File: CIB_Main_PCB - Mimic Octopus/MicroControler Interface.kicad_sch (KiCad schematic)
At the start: 3 parts

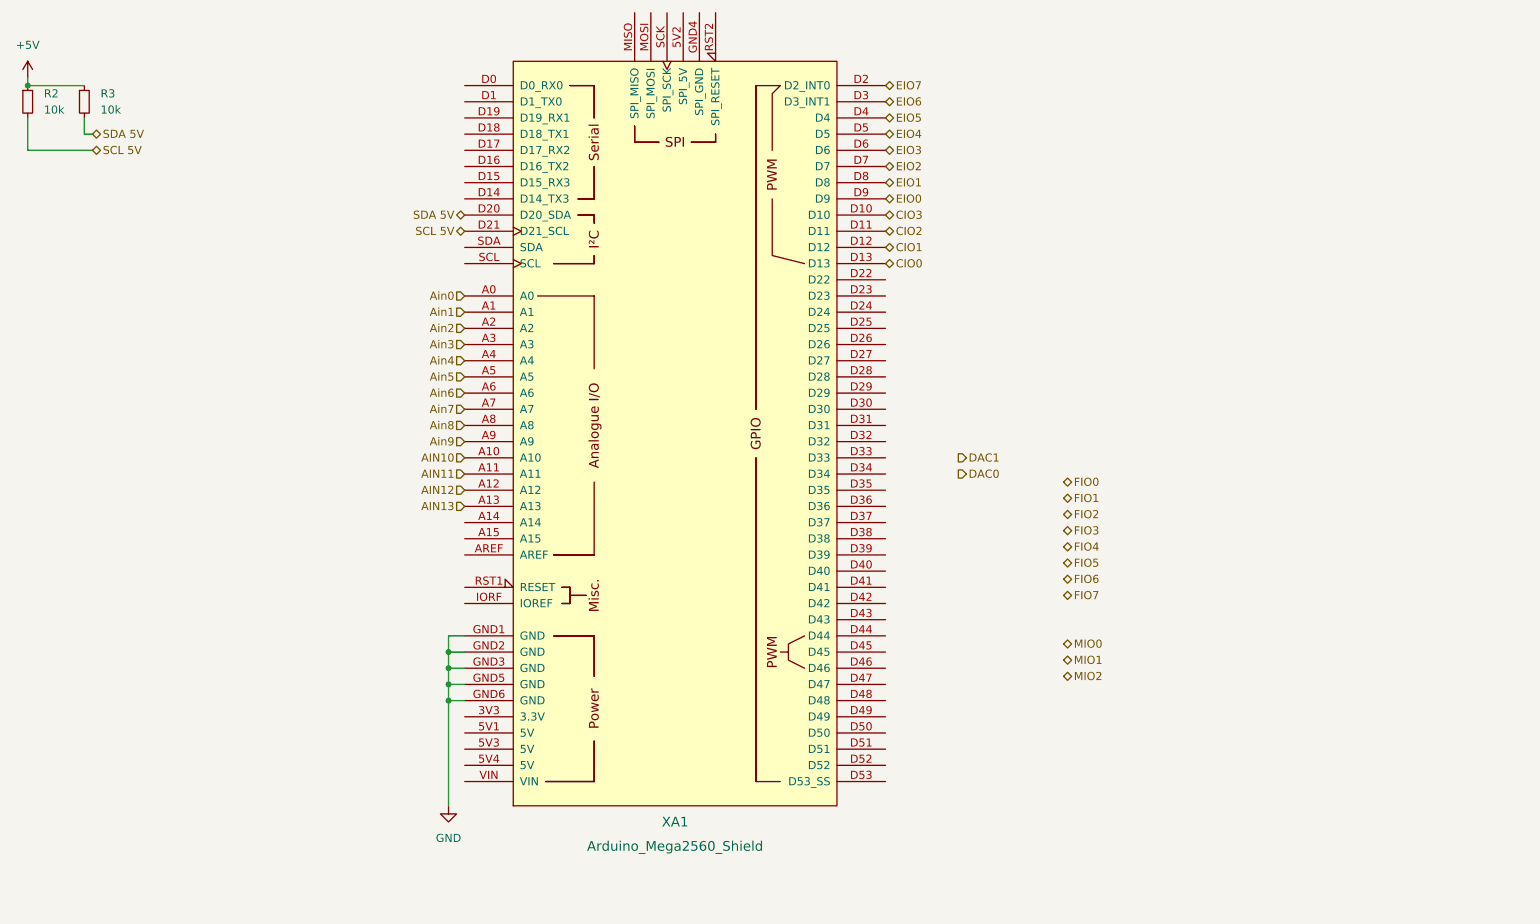
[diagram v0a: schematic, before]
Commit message: Added revision resistors
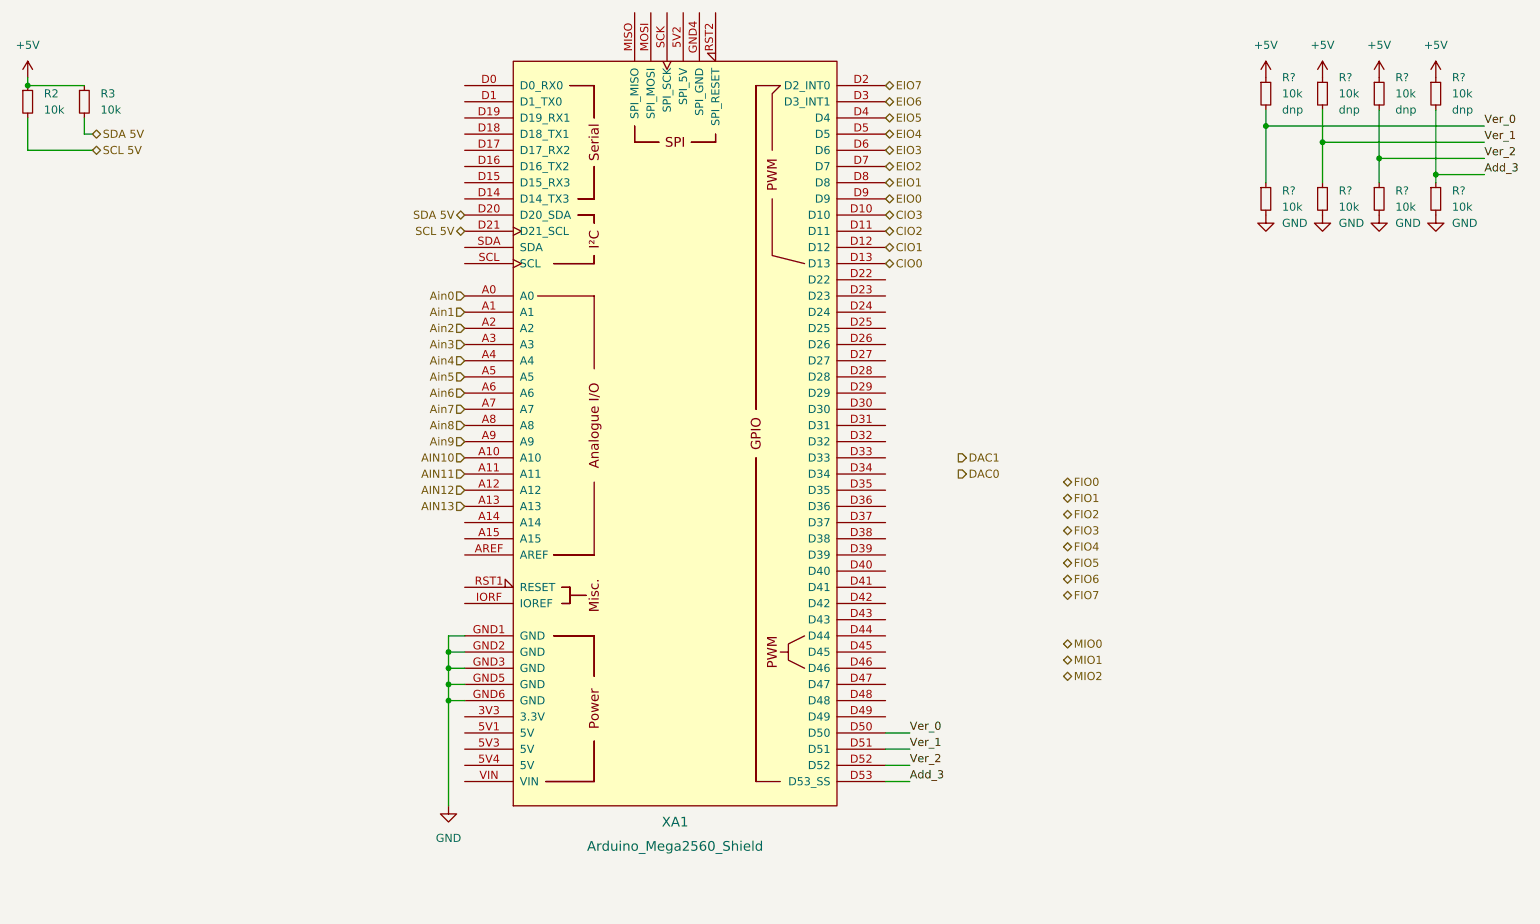
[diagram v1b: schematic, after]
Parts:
- added R? (x8): 10k, Resistor_SMD:R_1206_3216Metric_Pad1.30x1.75mm_HandSolder, symbol Device:R_Small
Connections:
- net +5V: now also R?.1, R?.1, R?.1, R?.1
- net GND: now also R?.2, R?.2, R?.2, R?.2
- net Ver_0: now reaches XA1.D50
- net Ver_0: now also R?.1, R?.2
- net Ver_1: now reaches XA1.D51
- net Ver_1: now also R?.1, R?.2
- net Ver_2: now reaches XA1.D52
- net Ver_2: now also R?.1, R?.2
- net Add_3: now reaches XA1.D53 (D53_SS)
- net Add_3: now also R?.1, R?.2

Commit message: added version resistors
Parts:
- gave numbers to parts that had none: 8
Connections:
- net Ver_0: now also XA1.D46; no longer XA1.D50
- net Ver_1: now also XA1.D48; no longer XA1.D51
- net Ver_2: now also XA1.D50; no longer XA1.D52
- net Add_3 renamed Ver_3
- net Ver_3: now also XA1.D52; no longer XA1.D53 (D53_SS)
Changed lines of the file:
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@@
+    (stroke (width 0) (type default) (color 0 0 0 0))
+  )
+  (wire (pts (xy 152.4 121.92) (xy 156.21 121.92))
     (stroke (width 0) (type default) (color 0 0 0 0))
   )
@@
     (stroke (width 0) (type default) (color 0 0 0 0))
   )
+  (wire (pts (xy 152.4 116.84) (xy 156.21 116.84))
+    (stroke (width 0) (type default) (color 0 0 0 0))
+  )
   (wire (pts (xy 83.82 121.92) (xy 86.36 121.92))
     (stroke (width 0) (type default) (color 0 0 0 0))
   )
-  (wire (pts (xy 152.4 129.54) (xy 156.21 129.54))
-    (stroke (width 0) (type default) (color 0 0 0 0))
-  )
   (wire (pts (xy 229.87 36.83) (xy 229.87 40.64))
     (stroke (width 0) (type default) (color 0 0 0 0))
@@
     (stroke (width 0) (type default) (color 0 0 0 0))
   )
-  (wire (pts (xy 152.4 134.62) (xy 156.21 134.62))
-    (stroke (width 0) (type default) (color 0 0 0 0))
-  )
   (wire (pts (xy 83.82 114.3) (xy 86.36 114.3))
     (stroke (width 0) (type default) (color 0 0 0 0))
@@
     (stroke (width 0) (type default) (color 0 0 0 0))
   )
-  (label "Ver_2" (at 156.21 132.08 0)
+  (label "Ver_2" (at 156.21 127 0)
     (effects (font (size 1.27 1.27)) (justify left bottom))
   )
-  (label "Add_3" (at 246.38 39.37 0)
+  (label "Ver_3" (at 246.38 39.37 0)
     (effects (font (size 1.27 1.27)) (justify left bottom))
   )
-  (label "Ver_0" (at 156.21 127 0)
+  (label "Ver_3" (at 156.21 132.08 0)
     (effects (font (size 1.27 1.27)) (justify left bottom))
   )
-  (label "Add_3" (at 156.21 134.62 0)
+  (label "Ver_0" (at 156.21 116.84 0)
     (effects (font (size 1.27 1.27)) (justify left bottom))
   )
@@
     (effects (font (size 1.27 1.27)) (justify left bottom))
   )
-  (label "Ver_1" (at 156.21 129.54 0)
+  (label "Ver_1" (at 156.21 121.92 0)
     (effects (font (size 1.27 1.27)) (justify left bottom))
   )
@@
   (symbol (lib_id "power:GND") (at 220.98 45.72 0) (unit 1)
     (in_bom yes) (on_board yes) (fields_autoplaced)
-    (property "Reference" "#PWR?" (id 0) (at 220.98 52.07 0)
+    (property "Reference" "#PWR0421" (id 0) (at 220.98 52.07 0)
       (effects (font (size 1.27 1.27)) hide)
     )
@@
   (symbol (lib_id "power:GND") (at 238.76 45.72 0) (unit 1)
     (in_bom yes) (on_board yes) (fields_autoplaced)
-    (property "Reference" "#PWR?" (id 0) (at 238.76 52.07 0)
+    (property "Reference" "#PWR0427" (id 0) (at 238.76 52.07 0)
       (effects (font (size 1.27 1.27)) hide)
     )
@@
   (symbol (lib_id "power:+5V") (at 238.76 24.13 0) (unit 1)
     (in_bom yes) (on_board yes) (fields_autoplaced)
-    (property "Reference" "#PWR?" (id 0) (at 238.76 27.94 0)
+    (property "Reference" "#PWR0422" (id 0) (at 238.76 27.94 0)
       (effects (font (size 1.27 1.27)) hide)
     )
@@
   (symbol (lib_id "Device:R_Small") (at 238.76 26.67 0) (unit 1)
     (in_bom yes) (on_board yes) (fields_autoplaced)
-    (property "Reference" "R?" (id 0) (at 241.3 24.1299 0)
+    (property "Reference" "R55" (id 0) (at 241.3 24.1299 0)
       (effects (font (size 1.27 1.27)) (justify left))
     )
@@
   (symbol (lib_id "Device:R_Small") (at 229.87 43.18 0) (unit 1)
     (in_bom yes) (on_board yes) (fields_autoplaced)
-    (property "Reference" "R?" (id 0) (at 232.41 41.9099 0)
+    (property "Reference" "R58" (id 0) (at 232.41 41.9099 0)
       (effects (font (size 1.27 1.27)) (justify left))
     )
@@
   (symbol (lib_id "power:+5V") (at 212.09 24.13 0) (unit 1)
     (in_bom yes) (on_board yes) (fields_autoplaced)
-    (property "Reference" "#PWR?" (id 0) (at 212.09 27.94 0)
+    (property "Reference" "#PWR0424" (id 0) (at 212.09 27.94 0)
       (effects (font (size 1.27 1.27)) hide)
     )
@@
   (symbol (lib_id "power:+5V") (at 220.98 24.13 0) (unit 1)
     (in_bom yes) (on_board yes) (fields_autoplaced)
-    (property "Reference" "#PWR?" (id 0) (at 220.98 27.94 0)
+    (property "Reference" "#PWR0423" (id 0) (at 220.98 27.94 0)
       (effects (font (size 1.27 1.27)) hide)
     )
@@
   (symbol (lib_id "power:GND") (at 229.87 45.72 0) (unit 1)
     (in_bom yes) (on_board yes) (fields_autoplaced)
-    (property "Reference" "#PWR?" (id 0) (at 229.87 52.07 0)
+    (property "Reference" "#PWR0426" (id 0) (at 229.87 52.07 0)
       (effects (font (size 1.27 1.27)) hide)
     )
@@
   (symbol (lib_id "power:GND") (at 212.09 45.72 0) (unit 1)
     (in_bom yes) (on_board yes) (fields_autoplaced)
-    (property "Reference" "#PWR?" (id 0) (at 212.09 52.07 0)
+    (property "Reference" "#PWR0420" (id 0) (at 212.09 52.07 0)
       (effects (font (size 1.27 1.27)) hide)
     )
@@
   (symbol (lib_id "Device:R_Small") (at 238.76 43.18 0) (unit 1)
     (in_bom yes) (on_board yes) (fields_autoplaced)
-    (property "Reference" "R?" (id 0) (at 241.3 41.9099 0)
+    (property "Reference" "R59" (id 0) (at 241.3 41.9099 0)
       (effects (font (size 1.27 1.27)) (justify left))
     )
@@
   (symbol (lib_id "Device:R_Small") (at 220.98 43.18 0) (unit 1)
     (in_bom yes) (on_board yes) (fields_autoplaced)
-    (property "Reference" "R?" (id 0) (at 223.52 41.9099 0)
+    (property "Reference" "R57" (id 0) (at 223.52 41.9099 0)
       (effects (font (size 1.27 1.27)) (justify left))
     )
@@
   (symbol (lib_id "Device:R_Small") (at 229.87 26.67 0) (unit 1)
     (in_bom yes) (on_board yes) (fields_autoplaced)
-    (property "Reference" "R?" (id 0) (at 232.41 24.1299 0)
+    (property "Reference" "R54" (id 0) (at 232.41 24.1299 0)
       (effects (font (size 1.27 1.27)) (justify left))
     )
@@
   (symbol (lib_id "Device:R_Small") (at 212.09 26.67 0) (unit 1)
     (in_bom yes) (on_board yes) (fields_autoplaced)
-    (property "Reference" "R?" (id 0) (at 214.63 24.1299 0)
+    (property "Reference" "R40" (id 0) (at 214.63 24.1299 0)
       (effects (font (size 1.27 1.27)) (justify left))
     )
@@
   (symbol (lib_id "Device:R_Small") (at 212.09 43.18 0) (unit 1)
     (in_bom yes) (on_board yes) (fields_autoplaced)
-    (property "Reference" "R?" (id 0) (at 214.63 41.9099 0)
+    (property "Reference" "R56" (id 0) (at 214.63 41.9099 0)
       (effects (font (size 1.27 1.27)) (justify left))
     )
@@
   (symbol (lib_id "Device:R_Small") (at 220.98 26.67 0) (unit 1)
     (in_bom yes) (on_board yes) (fields_autoplaced)
-    (property "Reference" "R?" (id 0) (at 223.52 24.1299 0)
+    (property "Reference" "R52" (id 0) (at 223.52 24.1299 0)
       (effects (font (size 1.27 1.27)) (justify left))
     )
@@
   (symbol (lib_id "power:+5V") (at 229.87 24.13 0) (unit 1)
     (in_bom yes) (on_board yes) (fields_autoplaced)
-    (property "Reference" "#PWR?" (id 0) (at 229.87 27.94 0)
-      (effects (font (size 1.27 1.27)) hide)
-    )
+    (property "Reference" "#PWR0425" (id 0) (at 229.87 27.94 0)
+      (effects (font (size 1.27 1.27)) hide)
+    )

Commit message: added changes
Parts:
- renumbered R40 to R1, R59 to R10, R52 to R2, R54 to R3, R55 to R4, R2 to R5, R3 to R6, R56 to R7, R57 to R8, R58 to R9
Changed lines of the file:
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@@
   (symbol (lib_id "power:GND") (at 220.98 45.72 0) (unit 1)
     (in_bom yes) (on_board yes) (fields_autoplaced)
-    (property "Reference" "#PWR0421" (id 0) (at 220.98 52.07 0)
+    (property "Reference" "#PWR038" (id 0) (at 220.98 52.07 0)
       (effects (font (size 1.27 1.27)) hide)
     )
@@
   (symbol (lib_id "power:GND") (at 238.76 45.72 0) (unit 1)
     (in_bom yes) (on_board yes) (fields_autoplaced)
-    (property "Reference" "#PWR0427" (id 0) (at 238.76 52.07 0)
+    (property "Reference" "#PWR040" (id 0) (at 238.76 52.07 0)
       (effects (font (size 1.27 1.27)) hide)
     )
@@
   (symbol (lib_id "Device:R_Small") (at 26.67 27.94 0) (unit 1)
     (in_bom yes) (on_board yes) (fields_autoplaced)
-    (property "Reference" "R3" (id 0) (at 29.21 26.6699 0)
+    (property "Reference" "R6" (id 0) (at 29.21 26.6699 0)
       (effects (font (size 1.27 1.27)) (justify left))
     )
@@
   (symbol (lib_id "power:+5V") (at 238.76 24.13 0) (unit 1)
     (in_bom yes) (on_board yes) (fields_autoplaced)
-    (property "Reference" "#PWR0422" (id 0) (at 238.76 27.94 0)
+    (property "Reference" "#PWR036" (id 0) (at 238.76 27.94 0)
       (effects (font (size 1.27 1.27)) hide)
     )
@@
   (symbol (lib_id "Device:R_Small") (at 17.78 27.94 0) (unit 1)
     (in_bom yes) (on_board yes) (fields_autoplaced)
-    (property "Reference" "R2" (id 0) (at 20.32 26.6699 0)
+    (property "Reference" "R5" (id 0) (at 20.32 26.6699 0)
       (effects (font (size 1.27 1.27)) (justify left))
     )
@@
   (symbol (lib_id "Device:R_Small") (at 238.76 26.67 0) (unit 1)
     (in_bom yes) (on_board yes) (fields_autoplaced)
-    (property "Reference" "R55" (id 0) (at 241.3 24.1299 0)
+    (property "Reference" "R4" (id 0) (at 241.3 24.1299 0)
       (effects (font (size 1.27 1.27)) (justify left))
     )
@@
   (symbol (lib_id "Device:R_Small") (at 229.87 43.18 0) (unit 1)
     (in_bom yes) (on_board yes) (fields_autoplaced)
-    (property "Reference" "R58" (id 0) (at 232.41 41.9099 0)
+    (property "Reference" "R9" (id 0) (at 232.41 41.9099 0)
       (effects (font (size 1.27 1.27)) (justify left))
     )
@@
   (symbol (lib_id "power:+5V") (at 212.09 24.13 0) (unit 1)
     (in_bom yes) (on_board yes) (fields_autoplaced)
-    (property "Reference" "#PWR0424" (id 0) (at 212.09 27.94 0)
+    (property "Reference" "#PWR033" (id 0) (at 212.09 27.94 0)
       (effects (font (size 1.27 1.27)) hide)
     )
@@
   (symbol (lib_id "power:+5V") (at 220.98 24.13 0) (unit 1)
     (in_bom yes) (on_board yes) (fields_autoplaced)
-    (property "Reference" "#PWR0423" (id 0) (at 220.98 27.94 0)
+    (property "Reference" "#PWR034" (id 0) (at 220.98 27.94 0)
       (effects (font (size 1.27 1.27)) hide)
     )
@@
   (symbol (lib_id "power:GND") (at 229.87 45.72 0) (unit 1)
     (in_bom yes) (on_board yes) (fields_autoplaced)
-    (property "Reference" "#PWR0426" (id 0) (at 229.87 52.07 0)
+    (property "Reference" "#PWR039" (id 0) (at 229.87 52.07 0)
       (effects (font (size 1.27 1.27)) hide)
     )
@@
   (symbol (lib_id "power:+5V") (at 17.78 24.13 0) (unit 1)
     (in_bom yes) (on_board yes) (fields_autoplaced)
-    (property "Reference" "#PWR019" (id 0) (at 17.78 27.94 0)
+    (property "Reference" "#PWR032" (id 0) (at 17.78 27.94 0)
       (effects (font (size 1.27 1.27)) hide)
     )
@@
   (symbol (lib_id "power:GND") (at 83.82 138.43 0) (unit 1)
     (in_bom yes) (on_board yes) (fields_autoplaced)
-    (property "Reference" "#PWR0376" (id 0) (at 83.82 144.78 0)
+    (property "Reference" "#PWR041" (id 0) (at 83.82 144.78 0)
       (effects (font (size 1.27 1.27)) hide)
     )
@@
   (symbol (lib_id "power:GND") (at 212.09 45.72 0) (unit 1)
     (in_bom yes) (on_board yes) (fields_autoplaced)
-    (property "Reference" "#PWR0420" (id 0) (at 212.09 52.07 0)
+    (property "Reference" "#PWR037" (id 0) (at 212.09 52.07 0)
       (effects (font (size 1.27 1.27)) hide)
     )
@@
   (symbol (lib_id "Device:R_Small") (at 238.76 43.18 0) (unit 1)
     (in_bom yes) (on_board yes) (fields_autoplaced)
-    (property "Reference" "R59" (id 0) (at 241.3 41.9099 0)
+    (property "Reference" "R10" (id 0) (at 241.3 41.9099 0)
       (effects (font (size 1.27 1.27)) (justify left))
     )
@@
   (symbol (lib_id "Device:R_Small") (at 220.98 43.18 0) (unit 1)
     (in_bom yes) (on_board yes) (fields_autoplaced)
-    (property "Reference" "R57" (id 0) (at 223.52 41.9099 0)
+    (property "Reference" "R8" (id 0) (at 223.52 41.9099 0)
       (effects (font (size 1.27 1.27)) (justify left))
     )
@@
   (symbol (lib_id "Device:R_Small") (at 229.87 26.67 0) (unit 1)
     (in_bom yes) (on_board yes) (fields_autoplaced)
-    (property "Reference" "R54" (id 0) (at 232.41 24.1299 0)
+    (property "Reference" "R3" (id 0) (at 232.41 24.1299 0)
       (effects (font (size 1.27 1.27)) (justify left))
     )
@@
   (symbol (lib_id "Device:R_Small") (at 212.09 26.67 0) (unit 1)
     (in_bom yes) (on_board yes) (fields_autoplaced)
-    (property "Reference" "R40" (id 0) (at 214.63 24.1299 0)
+    (property "Reference" "R1" (id 0) (at 214.63 24.1299 0)
       (effects (font (size 1.27 1.27)) (justify left))
     )
@@
   (symbol (lib_id "Device:R_Small") (at 212.09 43.18 0) (unit 1)
     (in_bom yes) (on_board yes) (fields_autoplaced)
-    (property "Reference" "R56" (id 0) (at 214.63 41.9099 0)
+    (property "Reference" "R7" (id 0) (at 214.63 41.9099 0)
       (effects (font (size 1.27 1.27)) (justify left))
     )
@@
   (symbol (lib_id "Device:R_Small") (at 220.98 26.67 0) (unit 1)
     (in_bom yes) (on_board yes) (fields_autoplaced)
-    (property "Reference" "R52" (id 0) (at 223.52 24.1299 0)
+    (property "Reference" "R2" (id 0) (at 223.52 24.1299 0)
       (effects (font (size 1.27 1.27)) (justify left))
     )
@@
   (symbol (lib_id "power:+5V") (at 229.87 24.13 0) (unit 1)
     (in_bom yes) (on_board yes) (fields_autoplaced)
-    (property "Reference" "#PWR0425" (id 0) (at 229.87 27.94 0)
-      (effects (font (size 1.27 1.27)) hide)
-    )
+    (property "Reference" "#PWR035" (id 0) (at 229.87 27.94 0)
+      (effects (font (size 1.27 1.27)) hide)
+    )

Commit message: V0.1 PCB to be sent out
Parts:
- added J17: LabJack1, Component Search Engine:Pluggable Terminal Blocks SDDC 1.5mm pitch 28 Pin, symbol Component Search Engine:Pluggable Terminal Blocks SDDC 1,5/ 14-PV-3,5
- added J18: Labjack2, Component Search Engine:Pluggable Terminal Blocks SDDC 1.5mm pitch 28 Pin, symbol Component Search Engine:Pluggable Terminal Blocks SDDC 1,5/ 14-PV-3,5
- XA1: footprint Arduino:Arduino_Mega2560_Shield -> _Arduino:Arduino_Mega2560_Shield
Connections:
- net +5V: now also J18.23, J18.9
- net AIN10: now also J18.3
- net AIN11: now also J18.4
- net AIN12: now also J18.5
- net AIN13: now also J18.6
- net Ain0: now also J18.22
- net Ain1: now also J18.21
- net Ain2: now also J18.20
- net Ain3: now also J18.19
- net Ain4: now also J18.18
- net Ain5: now also J18.17
- net Ain6: now also J18.16
- net Ain7: now also J18.15
- net Ain8: now also J18.1
- net Ain9: now also J18.2
- net CIO0: now also J17.12
- net CIO1: now also J17.11
- net CIO2: now also J17.10
- net CIO3: now also J17.9
- net EIO2: now also J17.8
- net EIO3: now also J17.7
- net EIO4: now also J17.6
- net EIO5: now also J17.5
- net GND: now also J17.13, J17.14, J17.27, J17.28, J18.10, J18.24
- net Ver_0: now also XA1.D53 (D53_SS); no longer XA1.D46
- net Ver_1: now also XA1.D52; no longer XA1.D48
- net Ver_2: now also XA1.D51; no longer XA1.D50
- net Ver_3: now also XA1.D50; no longer XA1.D52
- net AIN14: now reaches XA1.A14
- net AIN14: now also J18.7
- net AIN15: now reaches XA1.A15
- net AIN15: now also J18.8
- net Dout: now reaches XA1.D23
- net Dout: now also J17.1
- net Latch: now reaches XA1.D25
- net Latch: now also J17.3
- net Clock: now reaches XA1.D27
- net Clock: now also J17.2
